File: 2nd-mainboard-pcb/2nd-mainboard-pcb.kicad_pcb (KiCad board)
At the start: 4 copper layers, 99 x 97.5 mm, 132 parts, among them J1 PJ-082BH, J10 Servo Motor BL Touch, J11 T3, J12 Steckverbinder_Male_Fans, J13 Steckverbinder_Female_Leistung, J14 FAN3, J15 Steckverbinder_Female_Motoren, J16 ISP, J18 Quartz, J19 T2, J2 Fan_12/5V_Regelung, J20 T2, J21 T2, J22 T3, J23 Conn_01x04_Socket, J24 Steckverbinder_Male_Leistung, J3 Fan_12/5V_Regelung, J4 FAN0, J5 FAN1, J6 FAN2, J7 Stepper Motor, J8 Servo Motor SM, J9 Microstepping, P1 USB_C_Receptacle_USB2.0_14P, U1 SQJ409EP-T1_GE3, U10 ATmega328PB-A, U12 MPU-6050, U2 SZ1SMB5927BT3G, U3 TPS56837HRPAR, U4 TPS565208, U5 FT232RL, U6 PTS647SM38SMTR2LFS, U7 TPM16050-S6TR, U8 RJK0456DPB-00-J5, U9 RJK0456DPB-00-J5, Y1 ECS-160-18-4X-CKM

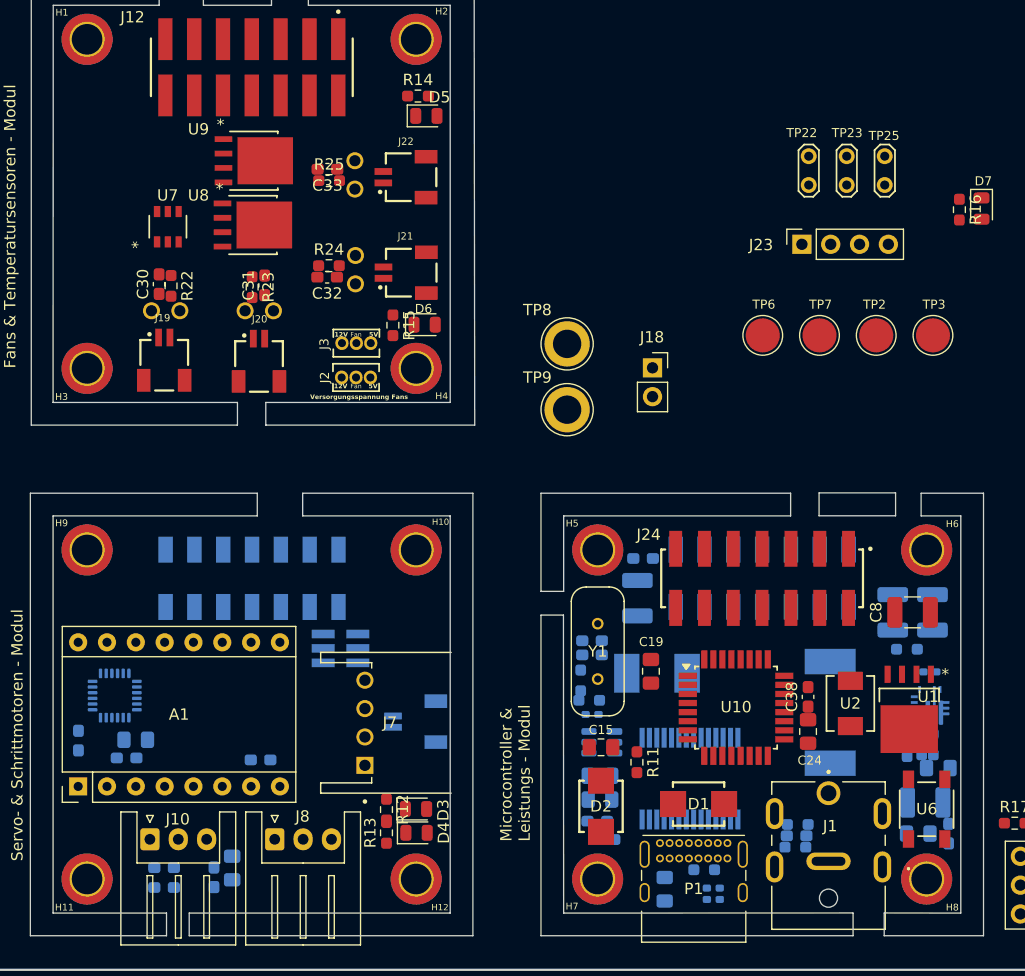
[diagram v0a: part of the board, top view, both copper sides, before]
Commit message: rearranged items a bit more, todo: fit item sizes to datasheets
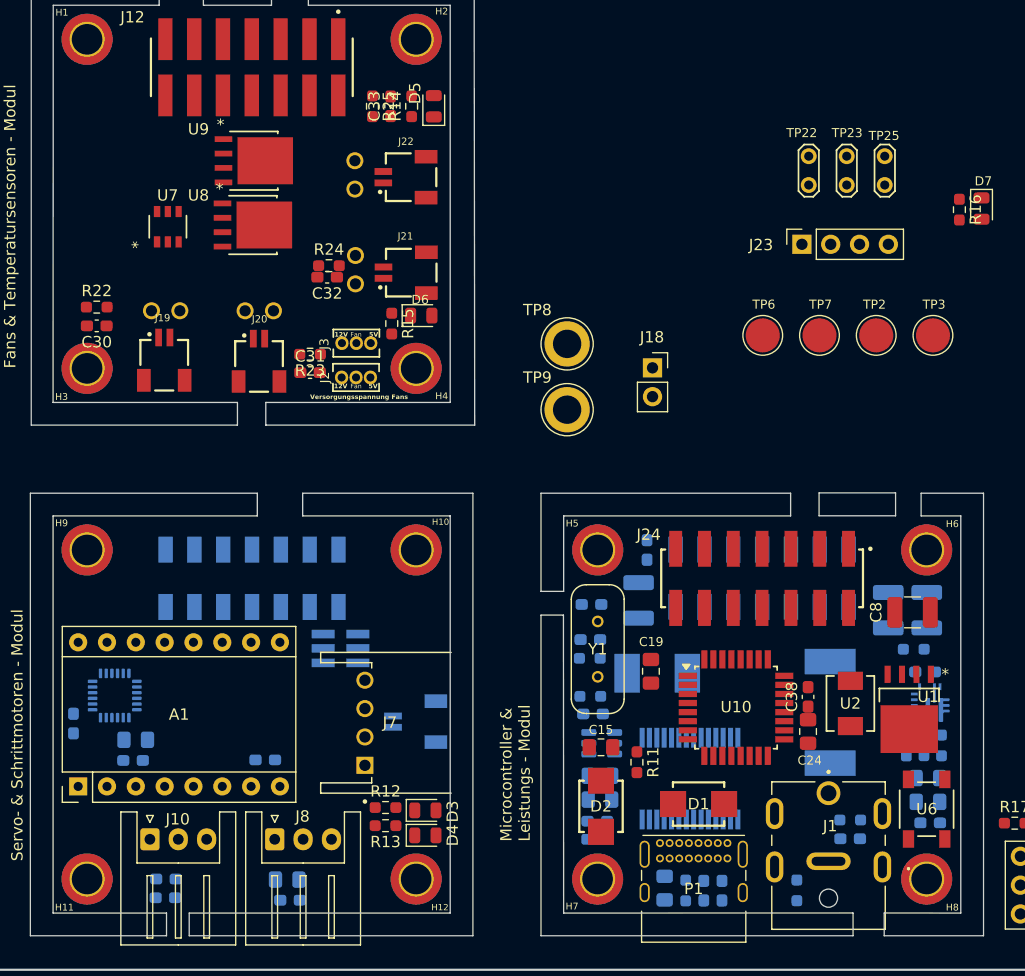
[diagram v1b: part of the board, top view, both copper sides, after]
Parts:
- removed C3: 10µF, Capacitor_SMD:C_0805_2012Metric_Pad1.18x1.45mm_HandSolder
- C1, C10, C16, C17: footprint Capacitor_SMD:C_0402_1005Metric_Pad0.74x0.62mm_HandSolder -> Capacitor_SMD:C_0603_1608Metric_Pad1.08x0.95mm_HandSolder
- C2: value 22nF -> 150pF
- C5: footprint Capacitor_SMD:C_1210_3225Metric_Pad1.33x2.70mm_HandSolder -> Capacitor_SMD:C_0805_2012Metric_Pad1.18x1.45mm_HandSolder
- moved C31 8.67 mm to (80.2, 97.4), turned to 0 degrees
- moved C33 7.86 mm to (87.2, 73.9), turned to 90 degrees
- moved R23 7.81 mm to (80.2, 95.8), turned to 180 degrees
- moved R25 7.58 mm to (85.7, 73.9), turned to -90 degrees
- moved C26 7.00 mm to (78.4, 143.9), turned to 180 degrees
- moved R22 6.81 mm to (61.4, 91.6), turned to 0 degrees
- moved C30 6.61 mm to (61.4, 93.3), turned to 180 degrees
- moved C25 4.96 mm to (78.1, 142.1), turned to 180 degrees
- moved C7 4.73 mm to (127.8, 138.4)
- moved R1 4.64 mm to (127.8, 136.8)
- moved C2 3.90 mm to (131.1, 118.3)
- moved R6 3.81 mm to (123.0, 143.0), turned to -90 degrees
- moved C22 3.20 mm to (105.0, 117.8)
- moved C9 3.01 mm to (134.5, 118.3)
- moved C4 2.93 mm to (134.6, 135.2)
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
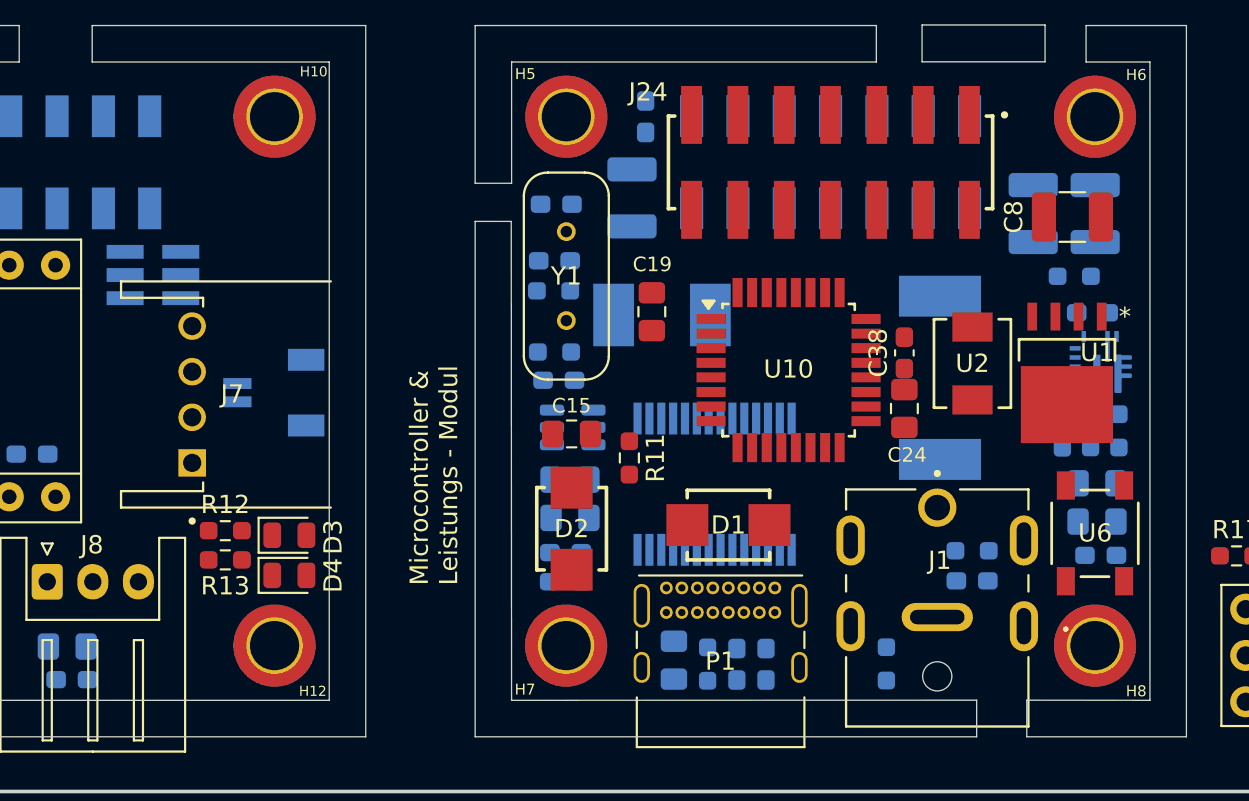
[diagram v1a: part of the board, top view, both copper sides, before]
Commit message: layout optimiert, kondensatoren angepasst
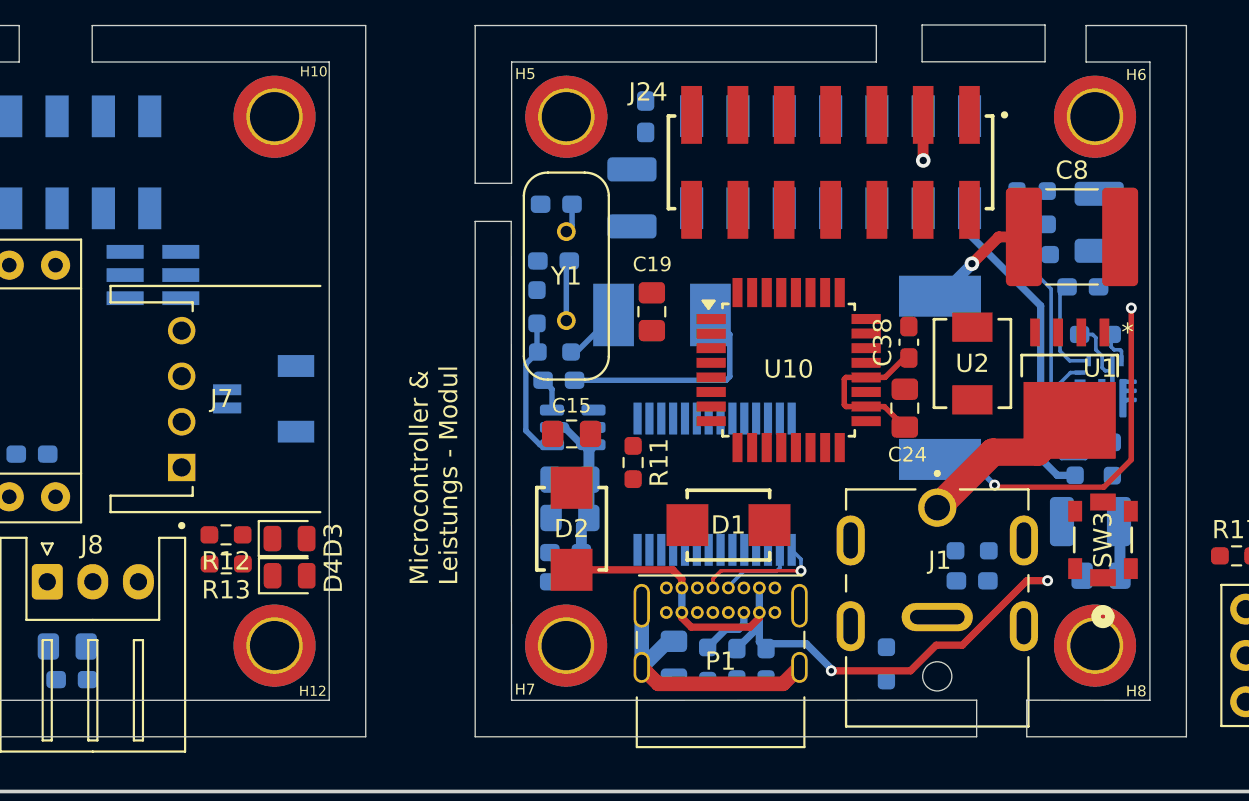
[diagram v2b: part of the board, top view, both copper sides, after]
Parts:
- removed U6: PTS647SM38SMTR2LFS, Imported_Component_Footprints:SW_PTS647SM38SMTR2LFS_CNK
- added SW3: PTS820 J25K SMTR LFS, Imported_Component_Footprints:PTS820 J25K SMTR LFS_CNK, F.Cu at (134.9, 136.2)
- C2, C9: footprint Capacitor_SMD:C_1210_3225Metric_Pad1.33x2.70mm_HandSolder -> Capacitor_SMD:C_0603_1608Metric_Pad1.08x0.95mm_HandSolder
- C4, C5: footprint Capacitor_SMD:C_0805_2012Metric_Pad1.18x1.45mm_HandSolder -> Capacitor_SMD:C_1210_3225Metric_Pad1.33x2.70mm_HandSolder
- C6: footprint Capacitor_SMD:C_0603_1608Metric_Pad1.08x0.95mm_HandSolder -> Capacitor_SMD:C_0805_2012Metric_Pad1.18x1.45mm_HandSolder
- C8: footprint Capacitor_SMD:C_1210_3225Metric_Pad1.33x2.70mm_HandSolder -> Capacitor_SMD:C_2220_5750Metric_Pad1.97x5.40mm_HandSolder
- moved C5 14.3 mm to (134.7, 118.8), turned to 90 degrees
- moved R4 10.2 mm to (131.1, 120.6), turned to 0 degrees
- moved C9 4.07 mm to (133.8, 122.3), turned to 0 degrees
- moved R3 4.04 mm to (131.9, 118.0), turned to -90 degrees
- moved R2 1.67 mm to (133.4, 131.8)
- moved R5 1.58 mm to (135.4, 131.8)
- moved U3 1.36 mm to (135.1, 127.8)
- moved R8 1.26 mm to (103.9, 123.4), turned to 90 degrees
- moved C1 1.20 mm to (134.5, 124.9)
- moved C6 1.12 mm to (134.8, 138.2)
- moved C8 1.09 mm to (133.2, 119.6), turned to 0 degrees
- moved C2 0.95 mm to (130.2, 118.0)
- moved U1 0.88 mm to (133.1, 128.4)
- moved J11 0.65 mm to (88.8, 128.5)
- moved C38 0.63 mm to (124.3, 125.4)
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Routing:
- net AREF: track 0.00 -> 64.4 mm, vias 0 -> 2
- net Net-(U3-SW): track 0.00 -> 23.4 mm, vias 0 -> 2
- net Net-(U3-FB): track 0.00 -> 22.3 mm
- net +12V: track 0.00 -> 17.3 mm, vias 0 -> 2
- net Net-(P1-SHIELD): track 0.00 -> 15.1 mm
- net Net-(U4-SW): track 0.00 -> 12.4 mm
- net +24V: track 0.00 -> 9.24 mm
- net Net-(U4-VFB): track 0.00 -> 7.93 mm
- net USBD+: track 0.00 -> 6.88 mm, vias 0 -> 1
- net Net-(U3-SS): track 0.00 -> 5.47 mm
- net GND: track 3.16 -> 8.26 mm
- net Net-(U3-PG): track 0.00 -> 4.93 mm
- net USBD-: track 0.00 -> 4.30 mm
- net Quartz_1: track 0.00 -> 3.34 mm
- net +5V_POW: track 0.00 -> 3.17 mm
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
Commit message: made some conns
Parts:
- C8: footprint Capacitor_SMD:C_2220_5750Metric_Pad1.97x5.40mm_HandSolder -> Capacitor_SMD:C_1812_4532Metric_Pad1.57x3.40mm_HandSolder
- moved C8 1.16 mm to (133.2, 118.4)
- moved C1 1.00 mm to (133.7, 124.3), turned to 90 degrees
- moved C9 0.88 mm to (133.2, 121.7)
- moved R4 0.73 mm to (130.9, 119.9)
- moved C2 0.67 mm to (130.0, 117.4)
- moved R3 0.66 mm to (131.8, 117.3)
- moved C5 0.61 mm to (134.3, 118.4)
- moved SW3 0.57 mm to (134.4, 136.3)
- moved U3 0.52 mm to (134.6, 128.0)
- moved U1 0.31 mm to (132.9, 128.7)
- moved C4 0.28 mm to (134.2, 135.5)
- moved R2 0.28 mm to (133.4, 132.0)
- moved R5 0.28 mm to (135.4, 132.0)
- moved U2 0.07 mm to (127.7, 126.5)
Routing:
- net PWR_IN_PROT: track 2.99 -> 21.1 mm, vias 0 -> 1
- net Net-(U3-FB): track 22.3 -> 7.72 mm
- net +24V: track 9.24 -> 0.00 mm
- net AREF: track 64.4 -> 71.3 mm
- net +12V: track 17.3 -> 11.4 mm, vias 2 -> 1
- net Net-(U3-MODE): track 2.62 -> 0.00 mm
- net Net-(U3-BOOT): track 1.87 -> 0.00 mm
